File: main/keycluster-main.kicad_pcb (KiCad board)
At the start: 2 copper layers, 45.1 x 52.6 mm, 36 parts, among them P2 CONN_5, P7 CONN_10, P8 CONN_7, SW1 S01_Socket, SW2 S01_Socket, SW3 S01_Socket, SW4 CMI126603D08, SW6 CMI126603D08, U1 MKL03Z32VFK4, U2 IS31FL3199, U4 ESD

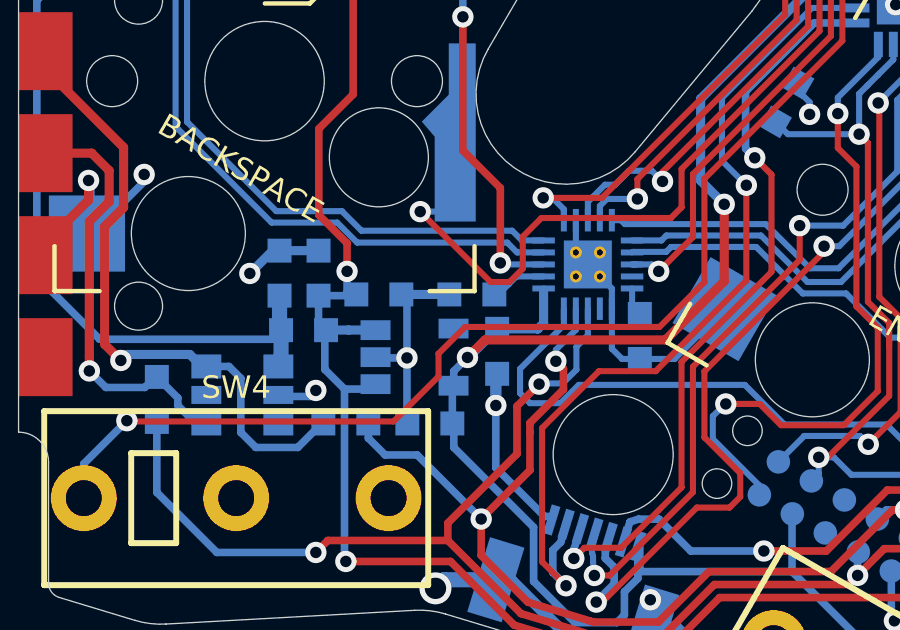
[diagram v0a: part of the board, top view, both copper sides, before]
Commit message: Connect IS31FL3199 to 5V instead of 3.3V
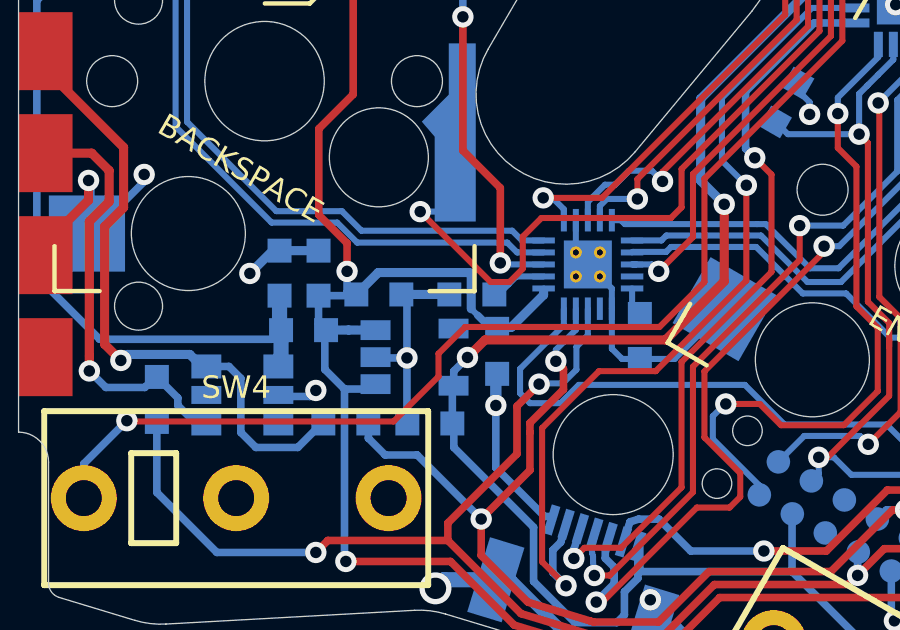
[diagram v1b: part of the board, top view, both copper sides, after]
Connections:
- C1 pad 2: +3V3 -> +5V
- U2 pad 1: +3V3 -> +5V
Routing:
- net +5V: track 122.1 -> 131.3 mm
- net +3V3: track 58.0 -> 53.7 mm

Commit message: Set R_EXT to 200K.
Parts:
- R4: value 20K -> 200K
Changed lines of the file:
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@@
     (at 145.709512 115.210302 90)
     (attr smd)
-    (fp_text reference R4 (at -1 1.45 180) (layer B.SilkS)
+    (fp_text reference R4 (at -0.9 1.5 180) (layer B.SilkS)
       (effects (font (size 0.75 0.75) (thickness 0.15)) (justify mirror))
     )
-    (fp_text value 20K (at -1.9 1.6 180) (layer B.SilkS)
+    (fp_text value 200K (at -1.9 1.6 180) (layer B.SilkS)
       (effects (font (size 0.75 0.75) (thickness 0.15)) (justify mirror))
     )

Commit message: Bump version to 3.1.0
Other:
- board text added: "PCB ID: keycluster_main_3.1.0"
- board text removed: "PCB ID: keycluster_main_3.0.0"
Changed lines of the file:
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@@
   (title_block
     (title "UHK Key Cluster Module - Main Board")
-    (rev 3.0.0)
+    (rev 3.1.0)
     (company "Ultimate Gadget Laboratories Kft.")
   )
@@
     (effects (font (size 0.75 0.75) (thickness 0.15)) (justify mirror))
   )
-  (gr_text "PCB ID:\nkeycluster_main_3.0.0" (at 162.493312 121.437542 60) (layer B.SilkS)
+  (gr_text "PCB ID:\nkeycluster_main_3.1.0" (at 162.493312 121.437542 60) (layer B.SilkS)
     (effects (font (size 0.75 0.75) (thickness 0.15)) (justify mirror))
   )
